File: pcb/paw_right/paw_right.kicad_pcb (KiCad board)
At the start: 2 copper layers, 141.8 x 96 mm, 44 parts, among them U1 Nice_Nano_V2

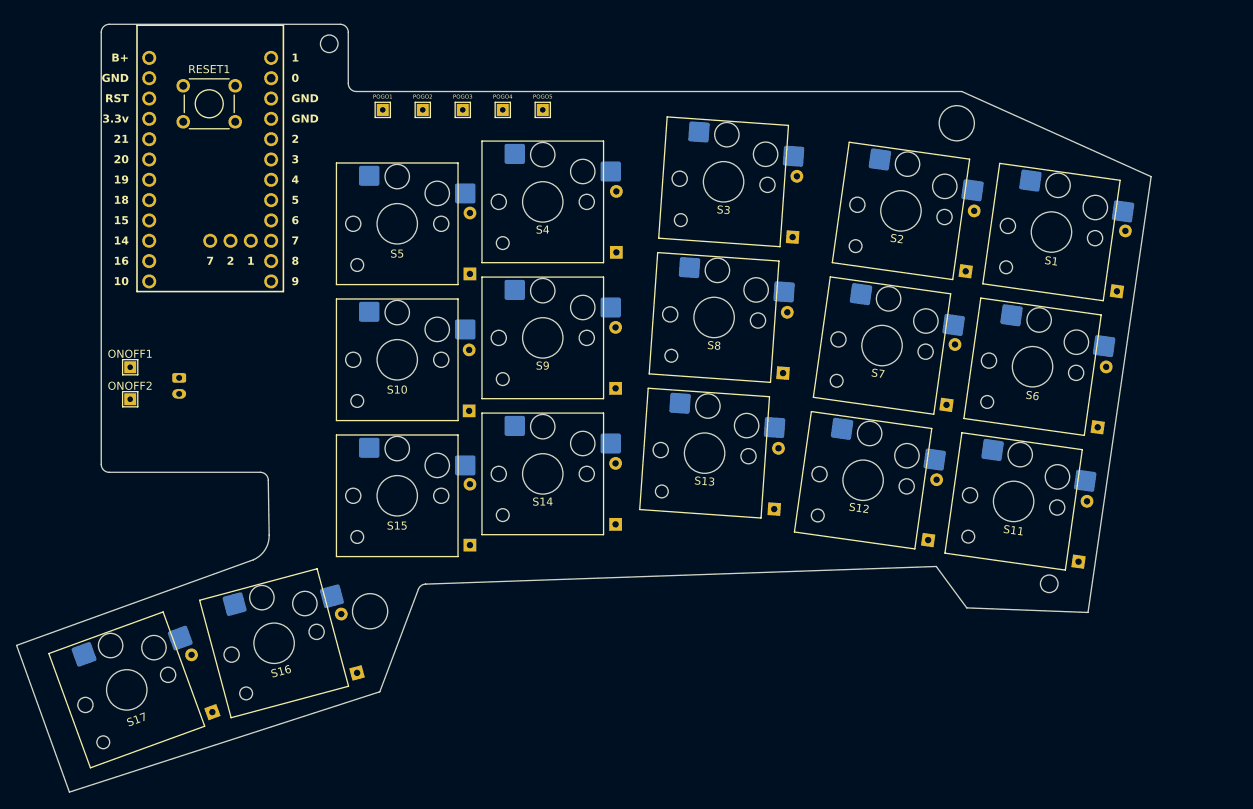
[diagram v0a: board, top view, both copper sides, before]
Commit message: Added tracks
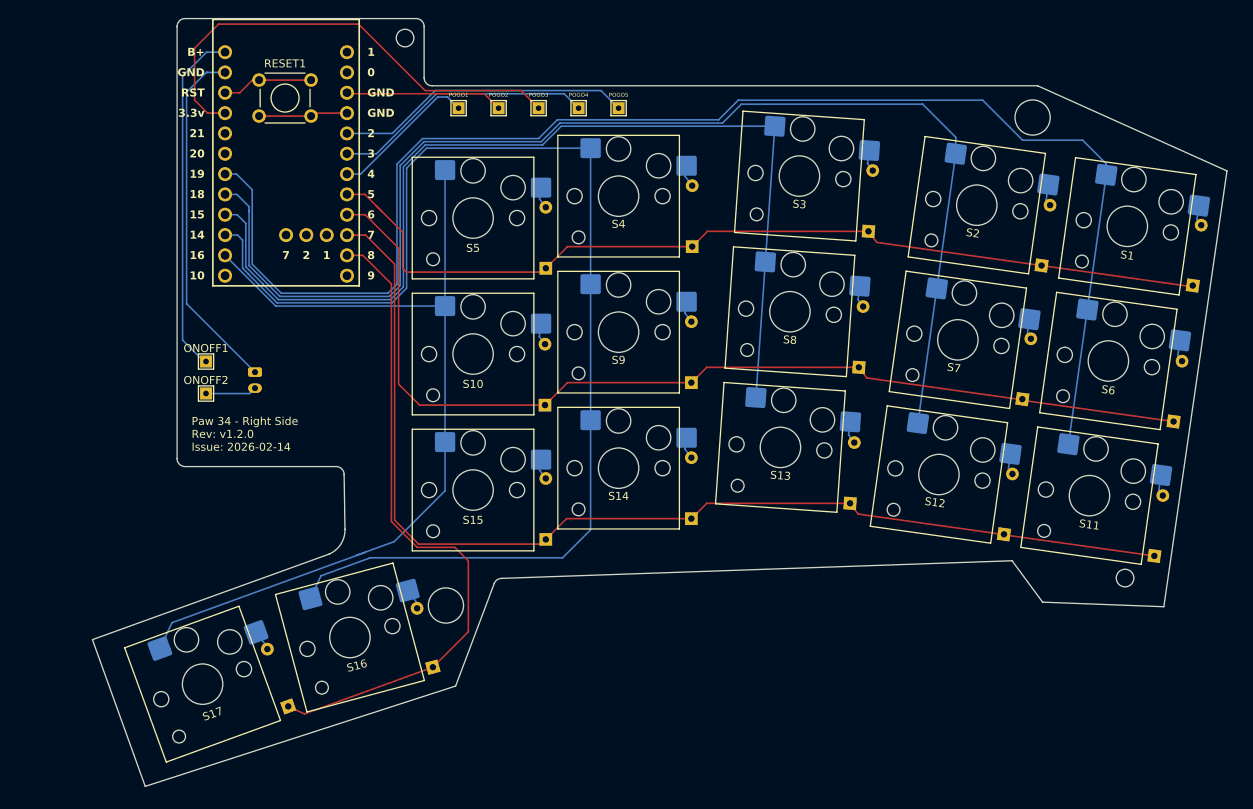
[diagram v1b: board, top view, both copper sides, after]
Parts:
- moved Battery1 9.51 mm to (96.7, 167.6)
- moved S6 9.51 mm to (203.4, 166.2)
- moved D15 9.51 mm to (133.1, 188.5)
- moved D2 9.51 mm to (195.0, 154.3)
- moved D6 9.51 mm to (211.5, 173.8)
- moved S5 9.51 mm to (124.0, 148.3)
- moved S14 9.51 mm to (142.2, 179.6)
- moved S3 9.51 mm to (164.8, 143.1)
- moved D9 9.51 mm to (151.3, 168.9)
- moved S2 9.51 mm to (186.9, 146.7)
- moved S8 9.51 mm to (163.6, 160.0)
- moved RESET1 9.51 mm to (97.2, 131.1)
- moved D13 9.51 mm to (171.1, 184.0)
- moved D14 9.51 mm to (151.3, 185.9)
- moved D10 9.51 mm to (133.0, 171.7)
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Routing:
- net Col 9: track 0.00 -> 179.2 mm
- net Col 8: track 0.00 -> 157.8 mm
- net Col 6: track 0.00 -> 154.4 mm
- net Row 2: track 0.00 -> 138.9 mm
- net Col 7: track 0.00 -> 128.1 mm
- net Row 1: track 0.00 -> 126.2 mm
- net Row 0: track 0.00 -> 116.7 mm
- net Col 5: track 0.00 -> 113.5 mm
- net Row 3: track 0.00 -> 82.8 mm
- net GND: track 0.00 -> 75.3 mm
- net 3V3: track 0.00 -> 59.6 mm
- net B+: track 0.00 -> 43.6 mm
- net SDA: track 0.00 -> 37.1 mm
- net SCL: track 0.00 -> 32.8 mm
- net RDY: track 0.00 -> 18.5 mm
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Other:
- board text added: "Paw 34 - Right Side Rev: ${REVISION} Issue: ${ISSUE_DATE}"

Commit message: PCB rev 1.2.0
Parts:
- added G***: LOGO, MentalDesk:Paw_Logo, F.Cu at (108.3, 175.3)
- moved D10 1.36 mm to (134.3, 171.5)
- moved D9 1.26 mm to (152.5, 168.7)
- moved D4 1.26 mm to (152.6, 151.7)
- moved S13 1.26 mm to (163.6, 176.8)
- moved S16 1.26 mm to (109.8, 200.5)
- moved D15 1.26 mm to (134.3, 188.3)
- moved D3 1.26 mm to (174.6, 149.8)
- moved D7 1.26 mm to (193.9, 170.7)
- moved D12 1.26 mm to (191.6, 187.6)
- moved S5 1.26 mm to (125.2, 148.1)
- moved S11 1.26 mm to (202.3, 182.8)
- moved ONOFF1 1.26 mm to (91.8, 166.0)
- moved D2 1.26 mm to (196.3, 154.0)
- moved RESET1 1.26 mm to (98.5, 130.8)
- moved S17 1.26 mm to (91.4, 206.3)
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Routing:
- net Row 3: track 82.8 -> 82.3 mm
